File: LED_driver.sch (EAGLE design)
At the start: 17 parts

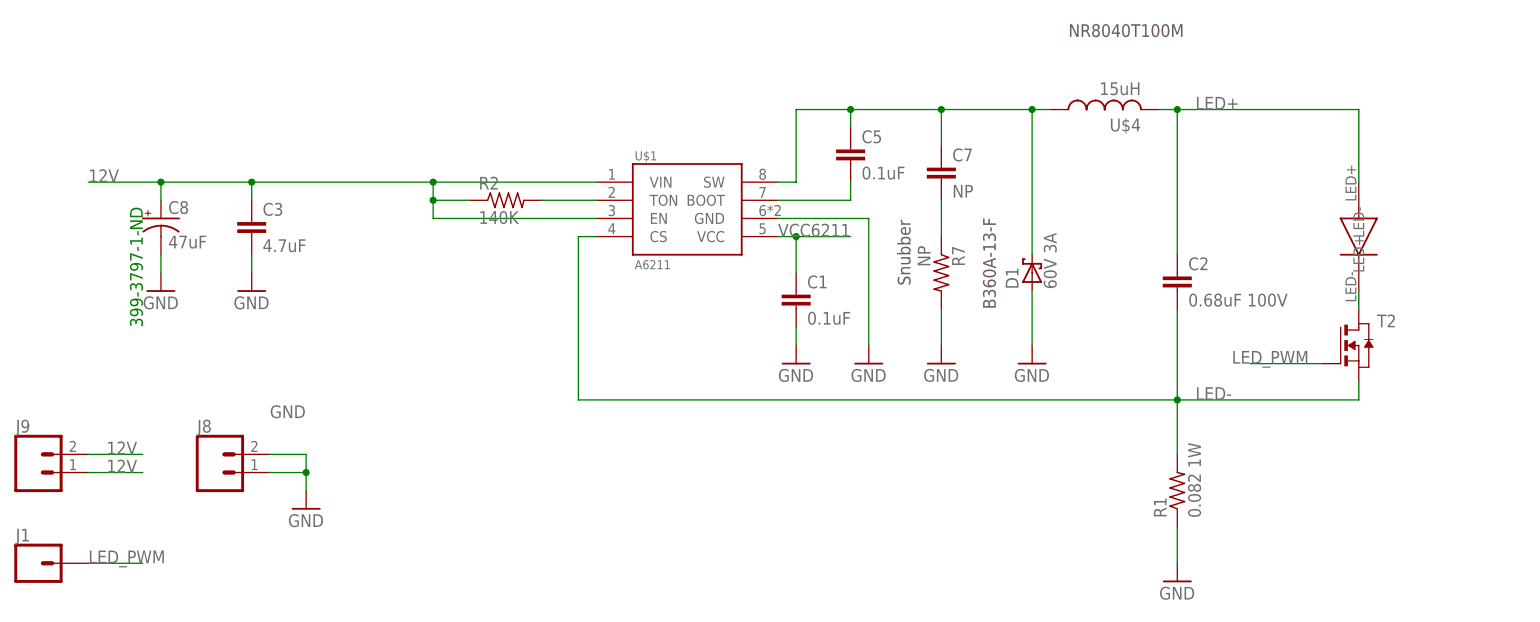
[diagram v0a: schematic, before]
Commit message: New revision with MOSFET connected to the Enable of the IC
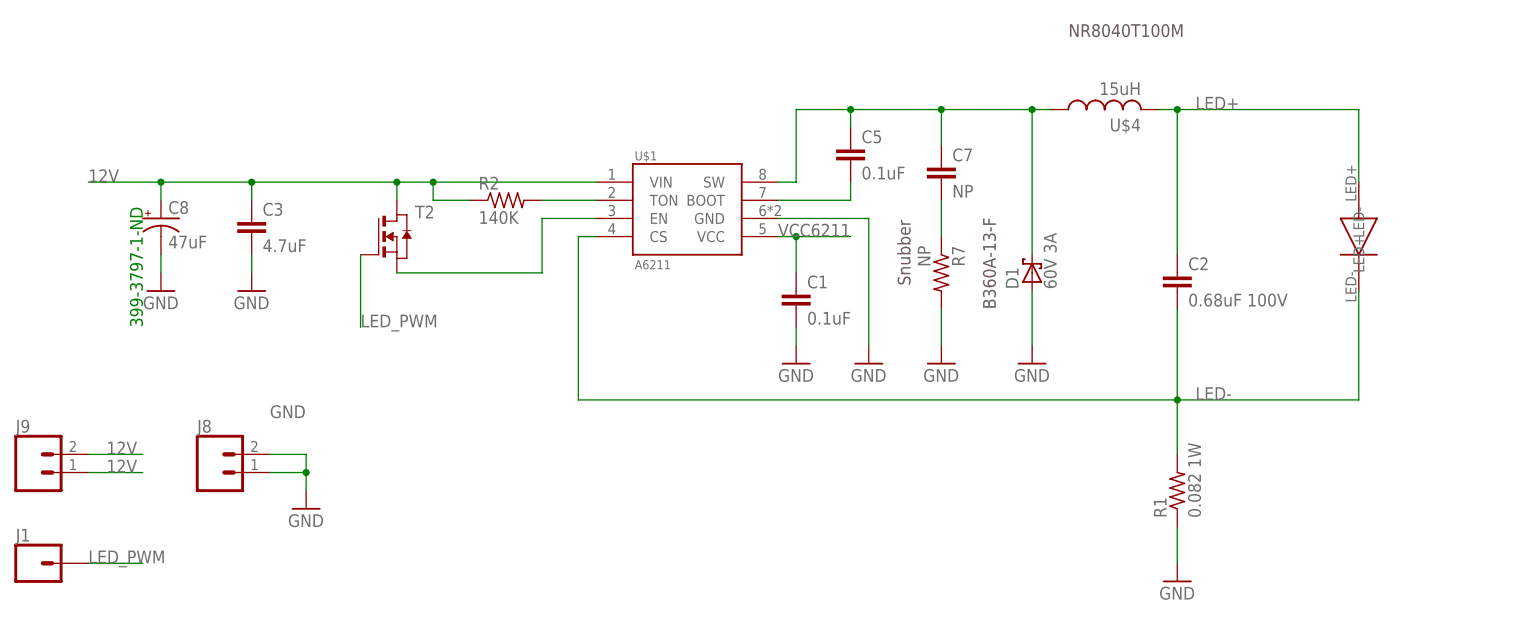
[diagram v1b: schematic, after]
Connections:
- removed net N$3: T2.D, U$3.LED-
- new net N$7: T2.S, U$1.EN
- net 12V: now also T2.D; no longer U$1.EN
- net LED-: now also U$3.LED-; no longer T2.S
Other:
- moved on the sheet: T2
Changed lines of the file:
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@@
 <?xml version="1.0" encoding="utf-8"?>
 <!DOCTYPE eagle SYSTEM "eagle.dtd">
-<eagle version="8.3.2">
+<eagle version="9.1.3">
 <drawing>
 <settings>
@@
 <instance part="J9" gate="G$1" x="45.72" y="81.28"/>
 <instance part="U$3" gate="G$1" x="231.14" y="114.3" rot="R270"/>
-<instance part="T2" gate="A" x="231.14" y="99.06"/>
+<instance part="T2" gate="A" x="96.52" y="114.3"/>
 </instances>
 <busses>
@@
 <pinref part="U$1" gate="G$1" pin="VIN"/>
 <wire x1="124.46" y1="121.92" x2="101.6" y2="121.92" width="0.1524" layer="91"/>
-<wire x1="101.6" y1="121.92" x2="76.2" y2="121.92" width="0.1524" layer="91"/>
+<wire x1="101.6" y1="121.92" x2="96.52" y2="121.92" width="0.1524" layer="91"/>
+<wire x1="96.52" y1="121.92" x2="76.2" y2="121.92" width="0.1524" layer="91"/>
 <wire x1="76.2" y1="121.92" x2="63.5" y2="121.92" width="0.1524" layer="91"/>
 <wire x1="63.5" y1="121.92" x2="53.34" y2="121.92" width="0.1524" layer="91"/>
@@
 <junction x="63.5" y="121.92"/>
 <pinref part="C3" gate="G$1" pin="1"/>
-<pinref part="U$1" gate="G$1" pin="EN"/>
-<wire x1="124.46" y1="116.84" x2="101.6" y2="116.84" width="0.1524" layer="91"/>
-<wire x1="101.6" y1="119.38" x2="101.6" y2="116.84" width="0.1524" layer="91"/>
-<junction x="101.6" y="119.38"/>
+<pinref part="T2" gate="A" pin="D"/>
+<wire x1="96.52" y1="119.38" x2="96.52" y2="121.92" width="0.1524" layer="91"/>
+<junction x="96.52" y="121.92"/>
 </segment>
 <segment>
@@
 <label x="208.28" y="91.44" size="1.778" layer="95"/>
 <wire x1="231.14" y1="91.44" x2="205.74" y2="91.44" width="0.1524" layer="91"/>
-<pinref part="T2" gate="A" pin="S"/>
-<wire x1="231.14" y1="93.98" x2="231.14" y2="91.44" width="0.1524" layer="91"/>
+<pinref part="U$3" gate="G$1" pin="LED-"/>
+<wire x1="231.14" y1="91.44" x2="231.14" y2="106.68" width="0.1524" layer="91"/>
 </segment>
 </net>
@@
 <segment>
 <pinref part="T2" gate="A" pin="G"/>
-<wire x1="226.06" y1="96.52" x2="215.9" y2="96.52" width="0.1524" layer="91"/>
-<label x="213.36" y="96.52" size="1.778" layer="95"/>
-</segment>
-</net>
-<net name="N$3" class="0">
-<segment>
-<pinref part="T2" gate="A" pin="D"/>
-<pinref part="U$3" gate="G$1" pin="LED-"/>
-<wire x1="231.14" y1="104.14" x2="231.14" y2="106.68" width="0.1524" layer="91"/>
-</segment>
-</net>
+<wire x1="91.44" y1="111.76" x2="91.44" y2="101.6" width="0.1524" layer="91"/>
+<label x="91.44" y="101.6" size="1.778" layer="95"/>
+</segment>
+</net>
+<net name="N$7" class="0">
+<segment>
+<pinref part="T2" gate="A" pin="S"/>
+<wire x1="96.52" y1="109.22" x2="116.84" y2="109.22" width="0.1524" layer="91"/>
+<pinref part="U$1" gate="G$1" pin="EN"/>
+<wire x1="116.84" y1="109.22" x2="116.84" y2="116.84" width="0.1524" layer="91"/>
+<wire x1="116.84" y1="116.84" x2="124.46" y2="116.84" width="0.1524" layer="91"/>
+</segment>
+</net>

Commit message: continued revisions
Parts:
- added J2, J3, J4, J5: (no value), SparkFun-Connectors:CONN_01
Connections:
- removed net N$7: T2.S, U$1.EN
- new net N$3: J4.1, J5.1, T2.D, U$3.LED-
- net 12V: now also U$1.EN; no longer T2.D
- net LED+: now also J2.1, J3.1
- net LED-: now also T2.S; no longer U$3.LED-
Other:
- moved on the sheet: T2
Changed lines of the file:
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@@
 <layer number="2" name="Route2" color="1" fill="3" visible="no" active="no"/>
 <layer number="3" name="Route3" color="4" fill="3" visible="no" active="no"/>
+<layer number="4" name="Route4" color="1" fill="4" visible="no" active="no"/>
+<layer number="5" name="Route5" color="4" fill="4" visible="no" active="no"/>
+<layer number="6" name="Route6" color="1" fill="8" visible="no" active="no"/>
+<layer number="7" name="Route7" color="4" fill="8" visible="no" active="no"/>
+<layer number="8" name="Route8" color="1" fill="2" visible="no" active="no"/>
+<layer number="9" name="Route9" color="4" fill="2" visible="no" active="no"/>
+<layer number="10" name="Route10" color="1" fill="7" visible="no" active="no"/>
+<layer number="11" name="Route11" color="4" fill="7" visible="no" active="no"/>
+<layer number="12" name="Route12" color="1" fill="5" visible="no" active="no"/>
+<layer number="13" name="Route13" color="4" fill="5" visible="no" active="no"/>
 <layer number="14" name="Route14" color="1" fill="6" visible="no" active="no"/>
 <layer number="15" name="Route15" color="4" fill="6" visible="no" active="no"/>
@@
 <part name="U$3" library="LED_00H53" deviceset="LED_00H53" device=""/>
 <part name="T2" library="zetex" deviceset="NMOSSOT23" device=""/>
+<part name="J2" library="SparkFun-Connectors" library_urn="urn:adsk.eagle:library:513" deviceset="CONN_01" device="" package3d_urn="urn:adsk.eagle:package:38028/1"/>
+<part name="J3" library="SparkFun-Connectors" library_urn="urn:adsk.eagle:library:513" deviceset="CONN_01" device="" package3d_urn="urn:adsk.eagle:package:38028/1"/>
+<part name="J4" library="SparkFun-Connectors" library_urn="urn:adsk.eagle:library:513" deviceset="CONN_01" device="" package3d_urn="urn:adsk.eagle:package:38028/1"/>
+<part name="J5" library="SparkFun-Connectors" library_urn="urn:adsk.eagle:library:513" deviceset="CONN_01" device="" package3d_urn="urn:adsk.eagle:package:38028/1"/>
 </parts>
 <sheets>
@@
 <instance part="J9" gate="G$1" x="45.72" y="81.28"/>
 <instance part="U$3" gate="G$1" x="231.14" y="114.3" rot="R270"/>
-<instance part="T2" gate="A" x="96.52" y="114.3"/>
+<instance part="T2" gate="A" x="231.14" y="96.52"/>
+<instance part="J2" gate="G$1" x="223.52" y="139.7"/>
+<instance part="J3" gate="G$1" x="241.3" y="139.7"/>
+<instance part="J4" gate="G$1" x="246.38" y="109.22"/>
+<instance part="J5" gate="G$1" x="246.38" y="93.98"/>
 </instances>
 <busses>
@@
 <wire x1="124.46" y1="121.92" x2="101.6" y2="121.92" width="0.1524" layer="91"/>
 <wire x1="101.6" y1="121.92" x2="96.52" y2="121.92" width="0.1524" layer="91"/>
-<wire x1="96.52" y1="121.92" x2="76.2" y2="121.92" width="0.1524" layer="91"/>
+<wire x1="96.52" y1="121.92" x2="93.98" y2="121.92" width="0.1524" layer="91"/>
+<wire x1="93.98" y1="121.92" x2="76.2" y2="121.92" width="0.1524" layer="91"/>
 <wire x1="76.2" y1="121.92" x2="63.5" y2="121.92" width="0.1524" layer="91"/>
 <wire x1="63.5" y1="121.92" x2="53.34" y2="121.92" width="0.1524" layer="91"/>
@@
 <junction x="63.5" y="121.92"/>
 <pinref part="C3" gate="G$1" pin="1"/>
-<pinref part="T2" gate="A" pin="D"/>
-<wire x1="96.52" y1="119.38" x2="96.52" y2="121.92" width="0.1524" layer="91"/>
-<junction x="96.52" y="121.92"/>
+<pinref part="U$1" gate="G$1" pin="EN"/>
+<wire x1="116.84" y1="116.84" x2="124.46" y2="116.84" width="0.1524" layer="91"/>
+<wire x1="116.84" y1="116.84" x2="93.98" y2="116.84" width="0.1524" layer="91"/>
+<wire x1="93.98" y1="116.84" x2="93.98" y2="121.92" width="0.1524" layer="91"/>
+<junction x="93.98" y="121.92"/>
 </segment>
 <segment>
@@
 <wire x1="205.74" y1="132.08" x2="231.14" y2="132.08" width="0.1524" layer="91"/>
 <wire x1="231.14" y1="132.08" x2="231.14" y2="121.92" width="0.1524" layer="91"/>
+<pinref part="J2" gate="G$1" pin="1"/>
+<wire x1="231.14" y1="132.08" x2="231.14" y2="139.7" width="0.1524" layer="91"/>
+<junction x="231.14" y="132.08"/>
+<pinref part="J3" gate="G$1" pin="1"/>
+<wire x1="231.14" y1="132.08" x2="248.92" y2="132.08" width="0.1524" layer="91"/>
+<wire x1="248.92" y1="132.08" x2="248.92" y2="139.7" width="0.1524" layer="91"/>
 </segment>
 </net>
@@
 <wire x1="121.92" y1="114.3" x2="124.46" y2="114.3" width="0.1524" layer="91"/>
 <label x="208.28" y="91.44" size="1.778" layer="95"/>
-<wire x1="231.14" y1="91.44" x2="205.74" y2="91.44" width="0.1524" layer="91"/>
-<pinref part="U$3" gate="G$1" pin="LED-"/>
-<wire x1="231.14" y1="91.44" x2="231.14" y2="106.68" width="0.1524" layer="91"/>
+<pinref part="T2" gate="A" pin="S"/>
+<wire x1="205.74" y1="91.44" x2="231.14" y2="91.44" width="0.1524" layer="91"/>
 </segment>
 </net>
@@
 <segment>
 <pinref part="T2" gate="A" pin="G"/>
-<wire x1="91.44" y1="111.76" x2="91.44" y2="101.6" width="0.1524" layer="91"/>
-<label x="91.44" y="101.6" size="1.778" layer="95"/>
-</segment>
-</net>
-<net name="N$7" class="0">
-<segment>
-<pinref part="T2" gate="A" pin="S"/>
-<wire x1="96.52" y1="109.22" x2="116.84" y2="109.22" width="0.1524" layer="91"/>
-<pinref part="U$1" gate="G$1" pin="EN"/>
-<wire x1="116.84" y1="109.22" x2="116.84" y2="116.84" width="0.1524" layer="91"/>
-<wire x1="116.84" y1="116.84" x2="124.46" y2="116.84" width="0.1524" layer="91"/>
-</segment>
-</net>
+<wire x1="226.06" y1="93.98" x2="226.06" y2="96.52" width="0.1524" layer="91"/>
+<label x="215.9" y="96.52" size="1.778" layer="95"/>
+</segment>
+</net>
+<net name="N$3" class="0">
+<segment>
+<pinref part="T2" gate="A" pin="D"/>
+<pinref part="U$3" gate="G$1" pin="LED-"/>
+<wire x1="231.14" y1="101.6" x2="231.14" y2="104.14" width="0.1524" layer="91"/>
+<pinref part="J4" gate="G$1" pin="1"/>
+<wire x1="231.14" y1="104.14" x2="231.14" y2="106.68" width="0.1524" layer="91"/>
+<wire x1="231.14" y1="104.14" x2="254" y2="104.14" width="0.1524" layer="91"/>
+<wire x1="254" y1="104.14" x2="254" y2="109.22" width="0.1524" layer="91"/>
+<junction x="231.14" y="104.14"/>
+<pinref part="J5" gate="G$1" pin="1"/>
+<wire x1="254" y1="93.98" x2="254" y2="104.14" width="0.1524" layer="91"/>
+<junction x="254" y="104.14"/>
+</segment>
+</net>
